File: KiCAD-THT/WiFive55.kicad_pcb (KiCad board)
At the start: 2 copper layers, 45.7 x 47.6 mm, 58 parts, among them J2 Switched Output, J3 Breadboard, J4 Grounds, J5 555-esque, K1 FINDER-36.11, Q1 BS170, Q2 IRF540N, Q5 BC557, SW3 PRG, SW6 RST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

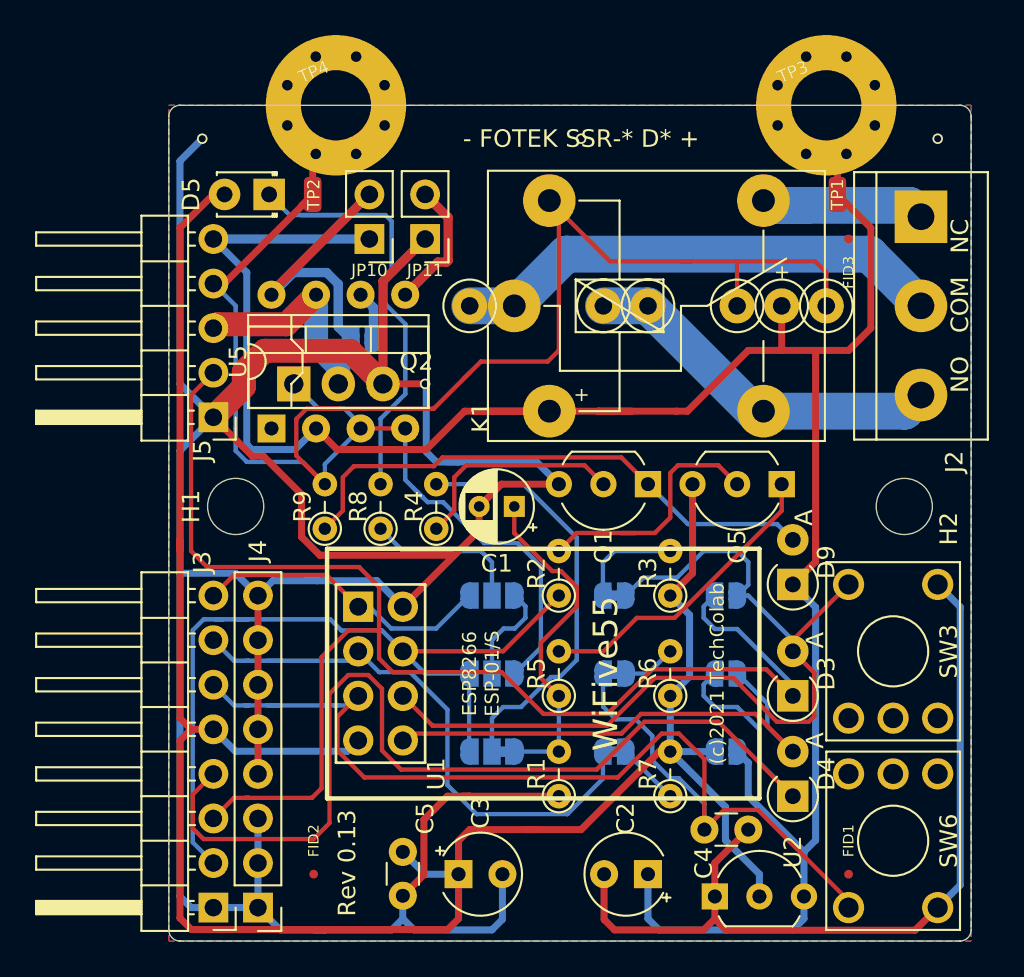
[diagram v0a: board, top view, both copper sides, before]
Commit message: Space for Omron G3MB-202P
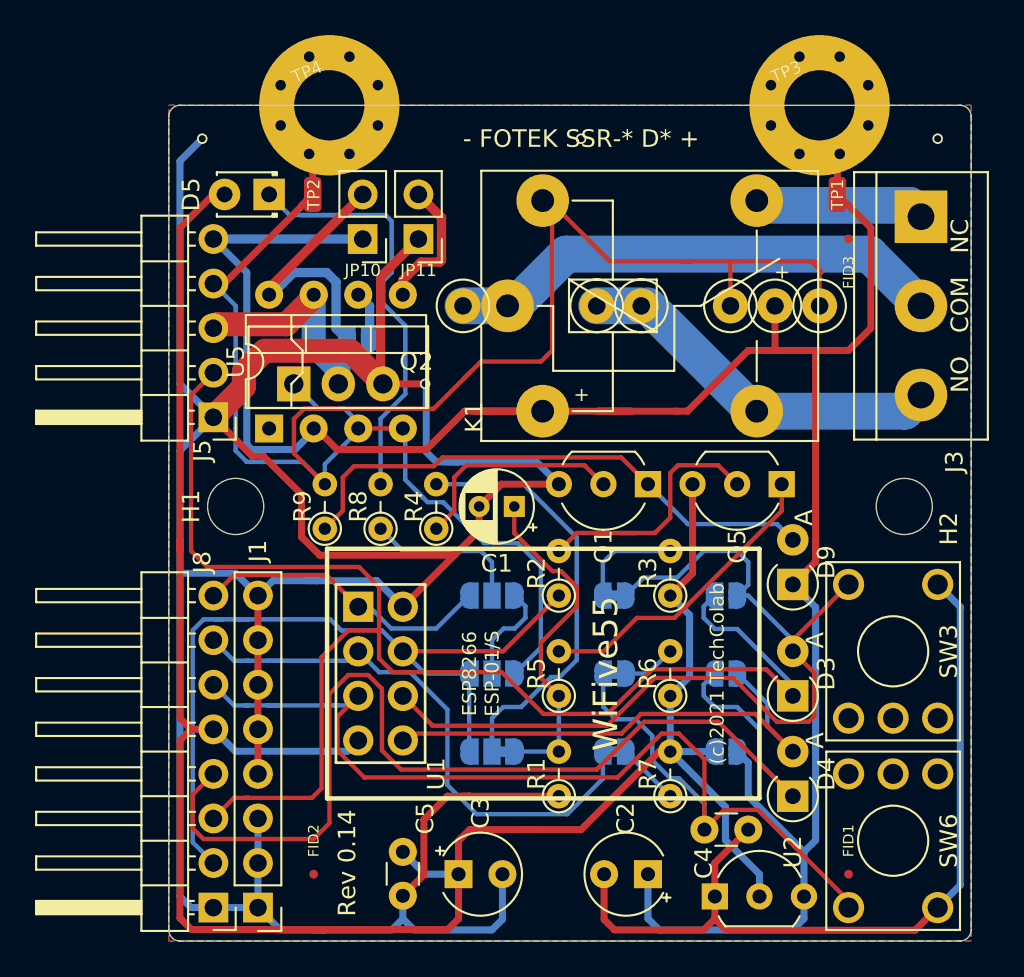
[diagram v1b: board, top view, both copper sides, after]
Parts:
- moved   0.38 mm to (137.4, 59.7)
- moved   0.38 mm to (134.9, 59.7)
- moved   0.38 mm to (132.3, 59.7)
- moved   0.38 mm to (127.3, 59.7)
- moved   0.38 mm to (124.7, 59.7)
- moved   0.38 mm to (117.1, 59.7)
- moved JP10 0.38 mm to (111.4, 55.9)
- moved JP11 0.38 mm to (114.6, 55.9)
- moved K1 0.38 mm to (119.6, 59.7)
- moved TP3 0.38 mm to (137.4, 48.3)
- moved TP4 0.38 mm to (109.5, 48.3)
- moved JP12 0.22 mm to (111.1, 61.6)
- moved U5 0.14 mm to (106.0, 66.7)
- renumbered J4 to J1, J2 to J3, J3 to J8
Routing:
- net /!OUT: track 117.7 -> 114.3 mm
- net (no net): track 0.00 -> 1.91 mm
- net /NC: track 11.0 -> 9.74 mm
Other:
- board text added: "Rev 0.14"
- board text removed: "Rev 0.13"

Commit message: update silks
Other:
- board text added: "N.ch d g s"
- board text added: "N.ch s d g"
- board text added: "PNP c b e"
- board text removed: "N.ch dgs"
- board text removed: "N.ch sdg"
- board text removed: "PNP cbe"
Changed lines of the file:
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@@
   (general
     (thickness 1.6)
-    (drawings 49)
+    (drawings 47)
     (tracks 489)
     (zones 0)
@@
     (0 F.Cu signal)
     (31 B.Cu signal)
-    (32 B.Adhes user hide)
-    (33 F.Adhes user hide)
-    (34 B.Paste user hide)
-    (35 F.Paste user hide)
+    (32 B.Adhes user)
+    (33 F.Adhes user)
+    (34 B.Paste user)
+    (35 F.Paste user)
     (36 B.SilkS user)
     (37 F.SilkS user)
-    (38 B.Mask user hide)
-    (39 F.Mask user hide)
-    (40 Dwgs.User user hide)
+    (38 B.Mask user)
+    (39 F.Mask user)
+    (40 Dwgs.User user)
     (41 Cmts.User user)
-    (42 Eco1.User user hide)
-    (43 Eco2.User user hide)
+    (42 Eco1.User user)
+    (43 Eco2.User user)
     (44 Edge.Cuts user)
     (45 Margin user)
     (46 B.CrtYd user)
     (47 F.CrtYd user)
-    (48 B.Fab user hide)
-    (49 F.Fab user hide)
+    (48 B.Fab user)
+    (49 F.Fab user)
   )
   (setup
-    (last_trace_width 2.1)
+    (last_trace_width 0.25)
     (user_trace_width 0.4)
     (user_trace_width 0.53)
@@
       (effects (font (size 1 1) (thickness 0.15)))
     )
-    (fp_text value TestPoint_Loop_D1.80mm_Drill1.0mm_Beaded (at 0 -2.8) (layer F.Fab)
+    (fp_text value TestPoint_Loop_D1.80mm_Drill1.0mm_Beaded (at -8.636 -20.32) (layer F.Fab)
       (effects (font (size 1 1) (thickness 0.15)))
     )
@@
       (effects (font (size 1 1) (thickness 0.15)))
     )
-    (fp_text value TestPoint_Loop_D1.80mm_Drill1.0mm_Beaded (at 0 -2.8) (layer F.Fab)
+    (fp_text value TestPoint_Loop_D1.80mm_Drill1.0mm_Beaded (at -5.588 -19.05) (layer F.Fab)
       (effects (font (size 1 1) (thickness 0.15)))
     )
@@
       (effects (font (size 1 1) (thickness 0.15)))
     )
-    (fp_text value TestPoint_Loop_D1.80mm_Drill1.0mm_Beaded (at 0 -2.8) (layer F.Fab)
+    (fp_text value TestPoint_Loop_D1.80mm_Drill1.0mm_Beaded (at -3.556 -19.812) (layer F.Fab)
       (effects (font (size 1 1) (thickness 0.15)))
     )
@@
       (effects (font (size 1 1) (thickness 0.15)))
     )
-    (fp_text value TestPoint_Loop_D1.80mm_Drill1.0mm_Beaded (at 0 -2.8) (layer F.Fab)
+    (fp_text value TestPoint_Loop_D1.80mm_Drill1.0mm_Beaded (at 1.778 -19.304) (layer F.Fab)
       (effects (font (size 1 1) (thickness 0.15)))
     )
@@
       (effects (font (size 1 1) (thickness 0.15)))
     )
-    (fp_text value TestPoint_Loop_D1.80mm_Drill1.0mm_Beaded (at 0 -2.8) (layer F.Fab)
+    (fp_text value TestPoint_Loop_D1.80mm_Drill1.0mm_Beaded (at 4.318 -20.066) (layer F.Fab)
       (effects (font (size 1 1) (thickness 0.15)))
     )
@@
       (effects (font (size 1 1) (thickness 0.15)))
     )
-    (fp_text value TestPoint_Loop_D1.80mm_Drill1.0mm_Beaded (at 0 -2.8) (layer F.Fab)
+    (fp_text value TestPoint_Loop_D1.80mm_Drill1.0mm_Beaded (at 12.192 -20.066) (layer F.Fab)
       (effects (font (size 1 1) (thickness 0.15)))
     )
@@
       (effects (font (size 1 1) (thickness 0.15)))
     )
-    (fp_text value 10 (at 1.25 3.5) (layer F.Fab)
+    (fp_text value 10 (at 1.016 1.651) (layer F.Fab)
       (effects (font (size 1 1) (thickness 0.15)))
     )
@@
       (effects (font (size 1 1) (thickness 0.15)))
     )
-    (fp_text value 10 (at 1.25 3.5) (layer F.Fab)
+    (fp_text value 10 (at 1.905 -1.397) (layer F.Fab)
       (effects (font (size 1 1) (thickness 0.15)))
     )
@@
       (effects (font (size 1 1) (thickness 0.15)))
     )
-    (fp_text value 4.7 (at 1 3.25) (layer F.Fab)
+    (fp_text value 4.7 (at 0.889 1.524) (layer F.Fab)
       (effects (font (size 1 1) (thickness 0.15)))
     )
@@
       (effects (font (size 1 1) (thickness 0.15)))
     )
-    (fp_text value 200 (at 1.27 1.27 90) (layer F.Fab)
+    (fp_text value 200 (at 2.032 0.254 90) (layer F.Fab)
       (effects (font (size 1 1) (thickness 0.15)))
     )
@@
       (effects (font (size 1 1) (thickness 0.15)))
     )
-    (fp_text value BC557 (at 2.54 2.79) (layer F.Fab)
+    (fp_text value BC557 (at 2.54 0) (layer F.Fab)
       (effects (font (size 1 1) (thickness 0.15)))
     )
@@
     (fp_arc (start 2.54 0) (end 2.54 -2.6) (angle -65) (layer F.SilkS) (width 0.12))
     (fp_arc (start 2.54 0) (end 0.74 1.85) (angle 20) (layer F.SilkS) (width 0.12))
-    (fp_text user %R (at 2.54 -3.56) (layer F.Fab)
+    (fp_text user %R (at 2.54 -2.032) (layer F.Fab)
       (effects (font (size 1 1) (thickness 0.15)))
     )
@@
       (effects (font (size 1 1) (thickness 0.15)))
     )
-    (fp_text value BS170 (at 2.54 2.79) (layer F.Fab)
+    (fp_text value BS170 (at 2.413 0) (layer F.Fab)
       (effects (font (size 1 1) (thickness 0.15)))
     )
@@
     (fp_arc (start 2.54 0) (end 2.54 -2.6) (angle -65) (layer F.SilkS) (width 0.12))
     (fp_arc (start 2.54 0) (end 0.74 1.85) (angle 20) (layer F.SilkS) (width 0.12))
-    (fp_text user %R (at 2.54 -3.56) (layer F.Fab)
+    (fp_text user %R (at 2.54 -2.032) (layer F.Fab)
       (effects (font (size 1 1) (thickness 0.15)))
     )
@@
       (effects (font (size 1 1) (thickness 0.15)))
     )
-    (fp_text value 470 (at 1.27 1.27 90) (layer F.Fab)
+    (fp_text value 470 (at 2.032 0.381 90) (layer F.Fab)
       (effects (font (size 1 1) (thickness 0.15)))
     )
@@
       (effects (font (size 1 1) (thickness 0.15)))
     )
-    (fp_text value 1N4148 (at 1.905 -0.635 90) (layer F.Fab)
+    (fp_text value 1N4148 (at 0.381 13.208 90) (layer F.Fab)
       (effects (font (size 1 1) (thickness 0.15)))
     )
@@
       (effects (font (size 1 1) (thickness 0.15)))
     )
-    (fp_text value "1N5817 Schottky" (at 0 -0.635 90) (layer F.Fab)
+    (fp_text value "1N5817 Schottky" (at -0.254 12.954 90) (layer F.Fab)
       (effects (font (size 1 1) (thickness 0.15)))
     )
@@
       (effects (font (size 1 1) (thickness 0.15)))
     )
-    (fp_text value "1N5817 Schottky" (at 1.27 -0.635 90) (layer F.Fab)
+    (fp_text value "1N5817 Schottky" (at 0.127 11.43 90) (layer F.Fab)
       (effects (font (size 1 1) (thickness 0.15)))
     )
@@
     )
   )
-  (gr_text "N.ch sdg" (at 117.23878 63.31204) (layer B.SilkS)
+  (gr_text "N.ch\n           s  d  g" (at 115.57 64.208) (layer B.SilkS)
     (effects (font (size 1 1) (thickness 0.15)) (justify mirror))
   )
@@
     (effects (font (size 1.2 1.2) (thickness 0.3)) (justify left))
   )
-  (gr_line (start 119.38 55.88) (end 129.54 43.18) (layer Dwgs.User) (width 0.15))
-  (gr_line (start 119.38 55.245) (end 119.38 55.88) (layer Dwgs.User) (width 0.15))
   (gr_text "- FOTEK SSR-* D* +" (at 123.825 50.165) (layer F.SilkS)
     (effects (font (size 1 1) (thickness 0.15)))
@@
   (gr_arc (start 100.965 95.25) (end 100.33 95.25) (angle -90) (layer Edge.Cuts) (width 0.05))
   (gr_arc (start 145.415 48.895) (end 146.05 48.895) (angle -90) (layer Edge.Cuts) (width 0.05))
-  (gr_text "N.ch\n\ndgs" (at 125.095 69.85) (layer B.SilkS)
+  (gr_text "N.ch\n\nd g s" (at 125.095 69.85) (layer B.SilkS)
     (effects (font (size 1 1) (thickness 0.15)) (justify mirror))
   )
-  (gr_text "PNP\n\ncbe" (at 132.715 69.85) (layer B.SilkS)
+  (gr_text "PNP\n\nc b e" (at 132.715 69.85) (layer B.SilkS)
     (effects (font (size 1 1) (thickness 0.15)) (justify mirror))
   )
@@
   (gr_line (start 100.33 95.25) (end 100.33 48.895) (layer Edge.Cuts) (width 0.05))
   (gr_line (start 146.05 48.895) (end 146.05 95.25) (layer Edge.Cuts) (width 0.05))
+  (segment (start 137.414 57.785) (end 137.414 59.69) (width 0.25) (layer F.Cu) (net 0))
   (segment (start 131.43 85.09) (end 128.905 85.09) (width 0.4) (layer B.Cu) (net 1) (status 30))
   (segment (start 128.905 85.09) (end 128.905 81.915) (width 0.4) (layer B.Cu) (net 1) (status 30))
@@
   (segment (start 132.715 57.15) (end 137.16 57.15) (width 0.25) (layer F.Cu) (net 9))
   (segment (start 137.541 57.785) (end 136.906 57.15) (width 0.25) (layer F.Cu) (net 9))
-  (segment (start 137.414 57.785) (end 137.414 59.69) (width 0.25) (layer F.Cu) (net 0))
   (segment (start 117.1575 63.8175) (end 115.425001 65.549999) (width 0.25) (layer F.Cu) (net 9))
   (segment (start 103.485002 58.42) (end 102.87 58.42) (width 0.4) (layer F.Cu) (net 9))
